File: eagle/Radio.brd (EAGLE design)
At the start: 100 x 80 mm, 105 parts, among them J500 2060-402, J501 2060-402, J920 2060-402, J921 2060-402, Q210 32.768kHz, Q610 32.768kHz, Q900 BSS123, U100 LP38693, U200 MSP430G2553, U300 IRF7103, U500 TPA2016D2, U900 EA_DOGMXXX-A, U910 PCA8574, U920 PCA9632TK, U930 IRF7309, U940 OPT3001, X100 2510-5, X110 2510-5

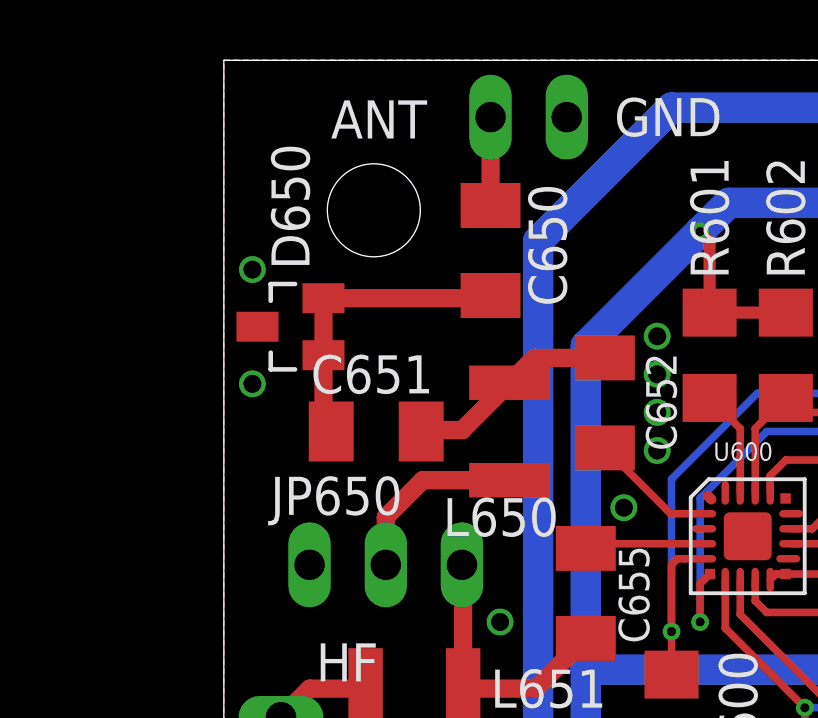
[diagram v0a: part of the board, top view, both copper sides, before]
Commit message: CHG: eagle schemetics and layout to solve issue with diode on antenna
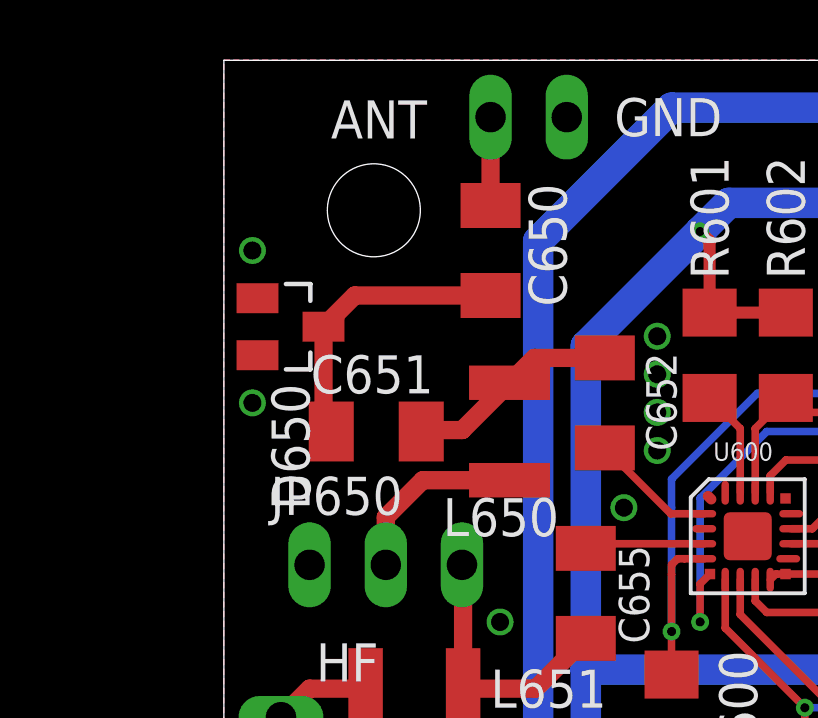
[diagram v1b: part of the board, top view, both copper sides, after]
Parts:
- turned D650 to 270 degrees
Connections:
- net GND: now also D650.1, D650.2; no longer D650.3
- net N$2: now also D650.3; no longer D650.1, D650.2
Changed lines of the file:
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@@
 <attribute name="VALUE" x="43.4975" y="35.8775" size="1.27" layer="27" rot="R180"/>
 </element>
-<element name="D650" library="diode" package="SOT23" value="BAT54S" x="2.2225" y="71.12" smashed="yes" rot="R90">
-<attribute name="NAME" x="2.8575" y="73.025" size="1.27" layer="25" rot="R90"/>
-<attribute name="VALUE" x="5.3975" y="69.215" size="1.27" layer="27" rot="R90"/>
+<element name="D650" library="diode" package="SOT23" value="BAT54S" x="2.2225" y="71.12" smashed="yes" rot="R270">
+<attribute name="NAME" x="1.5875" y="69.215" size="1.27" layer="25" rot="R270"/>
+<attribute name="VALUE" x="-0.9525" y="73.025" size="1.27" layer="27" rot="R270"/>
 </element>
 <element name="R901" library="rcl" package="R1206" value="1k" x="86.36" y="48.26" smashed="yes" rot="R270">
@@
 <via x="4.7625" y="50.4825" extent="1-16" drill="0.6" diameter="0.9"/>
 <via x="4.1275" y="51.435" extent="1-16" drill="0.6" diameter="0.9"/>
-<via x="0.9525" y="69.215" extent="1-16" drill="0.6" diameter="0.9"/>
+<via x="0.9525" y="68.58" extent="1-16" drill="0.6" diameter="0.9"/>
 <via x="80.3275" y="55.88" extent="1-16" drill="0.6" diameter="0.9"/>
 <via x="81.5975" y="55.245" extent="1-16" drill="0.6" diameter="0.9"/>
@@
 <contactref element="C654" pad="2"/>
 <contactref element="C653" pad="2"/>
-<contactref element="D650" pad="3"/>
 <contactref element="ANT" pad="1"/>
 <via x="4.1275" y="53.975" extent="1-16" drill="0.6" diameter="0.9"/>
@@
 <via x="14.44625" y="69.5325" extent="1-16" drill="0.6" diameter="0.9"/>
 <via x="10.795" y="39.37" extent="1-16" drill="0.6" diameter="0.9"/>
-<via x="0.9525" y="73.025" extent="1-16" drill="0.6" diameter="0.9"/>
+<via x="0.9525" y="73.66" extent="1-16" drill="0.6" diameter="0.9"/>
 <via x="7.3025" y="38.4175" extent="1-16" drill="0.6" diameter="0.9"/>
 <via x="8.5725" y="38.4175" extent="1-16" drill="0.6" diameter="0.9"/>
@@
 <contactref element="U940" pad="7"/>
 <wire x1="50" y1="23" x2="49.005" y2="23" width="0.254" layer="16"/>
+<contactref element="D650" pad="2"/>
+<contactref element="D650" pad="1"/>
 </signal>
 <signal name="+5V">
@@
 </signal>
 <signal name="N$2">
+<contactref element="C651" pad="2"/>
+<wire x1="3.58" y1="67.6275" x2="3.3225" y2="67.6275" width="0.6096" layer="1"/>
 <contactref element="C650" pad="2"/>
-<contactref element="D650" pad="2"/>
-<wire x1="3.3225" y1="72.07" x2="8.8" y2="72.07" width="0.6096" layer="1"/>
-<wire x1="8.8" y1="72.07" x2="8.89" y2="72.16" width="0.6096" layer="1"/>
-<contactref element="C651" pad="2"/>
-<contactref element="D650" pad="1"/>
+<contactref element="D650" pad="3"/>
 <wire x1="3.58" y1="67.6275" x2="3.3225" y2="67.6275" width="0.6096" layer="1"/>
-<wire x1="3.3225" y1="67.6275" x2="3.3225" y2="70.17" width="0.6096" layer="1"/>
-<wire x1="3.3225" y1="70.17" x2="3.3225" y2="72.07" width="0.6096" layer="1"/>
+<wire x1="3.3225" y1="67.6275" x2="3.3225" y2="71.12" width="0.6096" layer="1"/>
+<wire x1="3.3225" y1="71.12" x2="4.3625" y2="72.16" width="0.6096" layer="1"/>
+<wire x1="4.3625" y1="72.16" x2="8.89" y2="72.16" width="0.6096" layer="1"/>
 </signal>
 <signal name="N$32">

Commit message: CHG: Finishing Layout and Schemetics
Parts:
- added R921, R922, R923: 1k, rcl:R1206
- moved C920 10.4 mm to (92.4, 53.0), turned to 0 degrees
- moved U920 3.82 mm to (90.2, 48.3), turned to 0 degrees
- moved J920 0.32 mm to (91.1, 36.8)
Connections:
- new net N$25: R921.1, U920.2
- new net N$45: J920.B-2, R922.2
- new net N$46: J921.B-2, R923.2
- net +5V: no longer R901.1
- net GND: now also R901.1
- net N$3: now also R923.1, U920.4; no longer J920.B-1, U920.2
- net N$44: now also J920.B-1, R921.2; no longer J921.B-2, U920.4
- net N$5: now also R922.1; no longer J920.B-2
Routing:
- net N$25: track 0.00 -> 15.7 mm
- net N$46: track 0.00 -> 15.3 mm
- net N$3: track 15.6 -> 3.72 mm
- net N$44: track 15.5 -> 4.01 mm
- net +5V: track 386.2 -> 375.0 mm
- net SCL_5V: track 165.9 -> 177.0 mm
- net +5_PCA: track 71.3 -> 61.2 mm
- net SDA_5V: track 173.7 -> 183.7 mm
- net N$45: track 0.00 -> 4.95 mm
- net EN1_TAST: track 63.6 -> 62.9 mm
- net N$5: track 7.26 -> 6.60 mm
- net LCD_BACKLIGHT: track 5.46 -> 6.00 mm

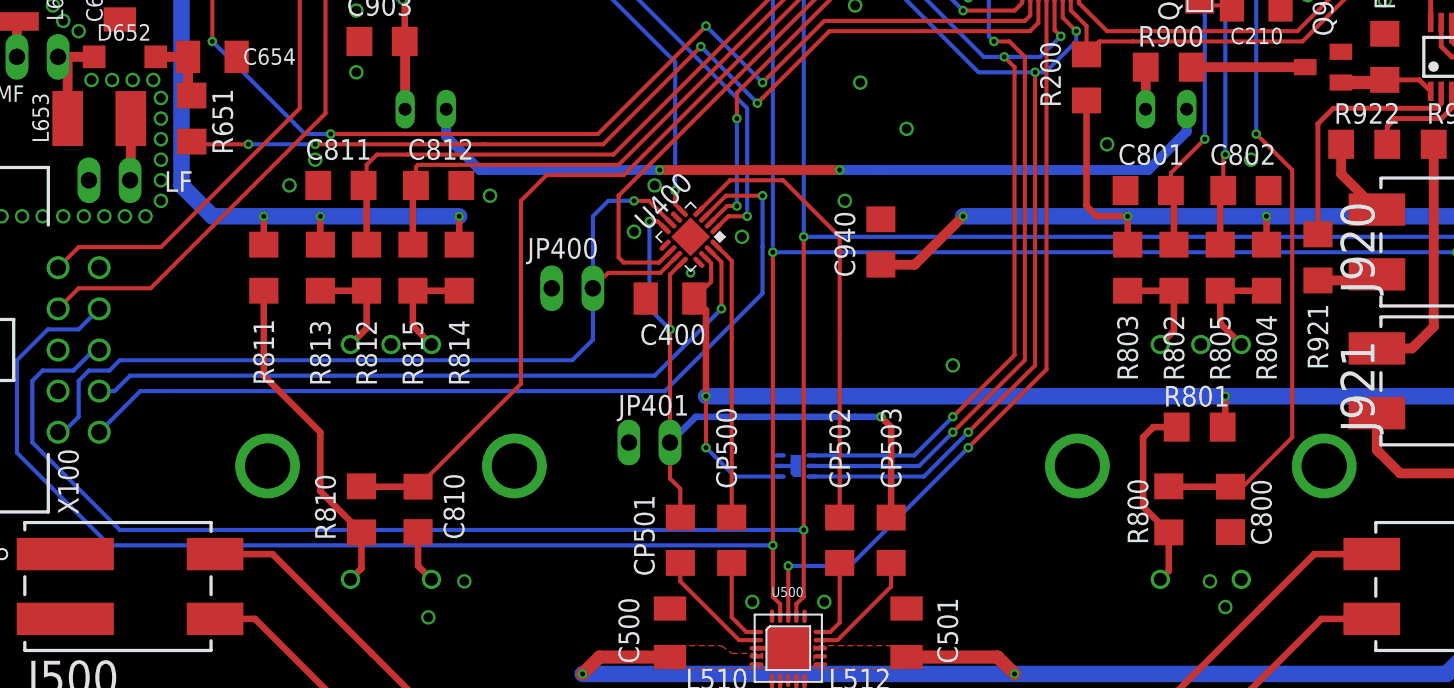
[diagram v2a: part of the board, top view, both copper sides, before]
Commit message: CHG: solved some problems on pcb updated encoder footprint, further updated schemetics and changed pull up resitor to an pull down for lcd backlight controll
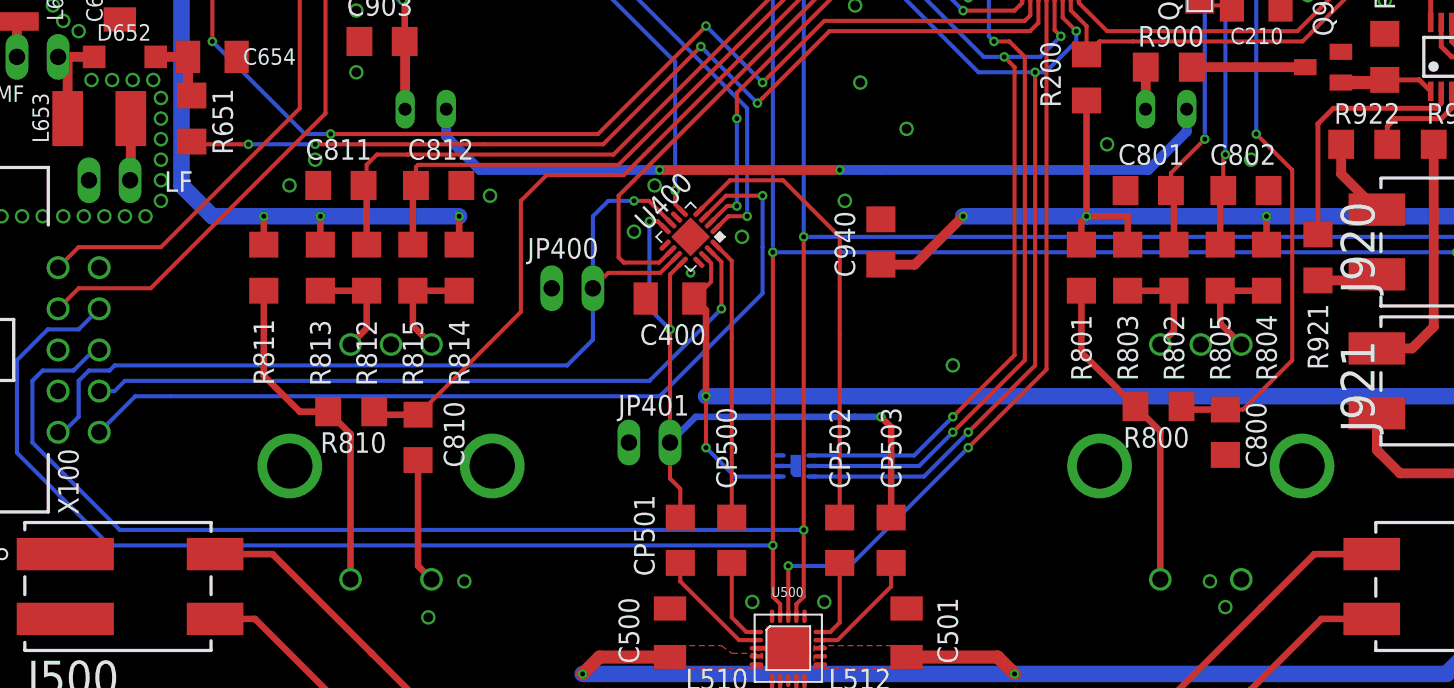
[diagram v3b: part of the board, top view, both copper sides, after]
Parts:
- U910: device Radio Projekt:TSSOP16 -> Radio Projekt:PCA8574_TSSOP16
- moved R801 12.3 mm to (67.6, 35.2), turned to 90 degrees
- moved R800 6.38 mm to (72.4, 26.7), turned to 180 degrees
- moved R810 6.07 mm to (22.5, 26.4), turned to 0 degrees
- moved C800 4.77 mm to (76.5, 25.1)
- moved C810 4.45 mm to (26.7, 24.8)
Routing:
- net N$36: track 12.0 -> 19.8 mm
- net EN1_TAST: track 62.9 -> 57.4 mm
- net EN2_TAST: track 60.6 -> 55.5 mm
- net GND: track 7.06 -> 11.5 mm
- net AUX_LIN: track 45.0 -> 44.4 mm
- net +3V3: track 396.9 -> 397.2 mm, vias 15 -> 14

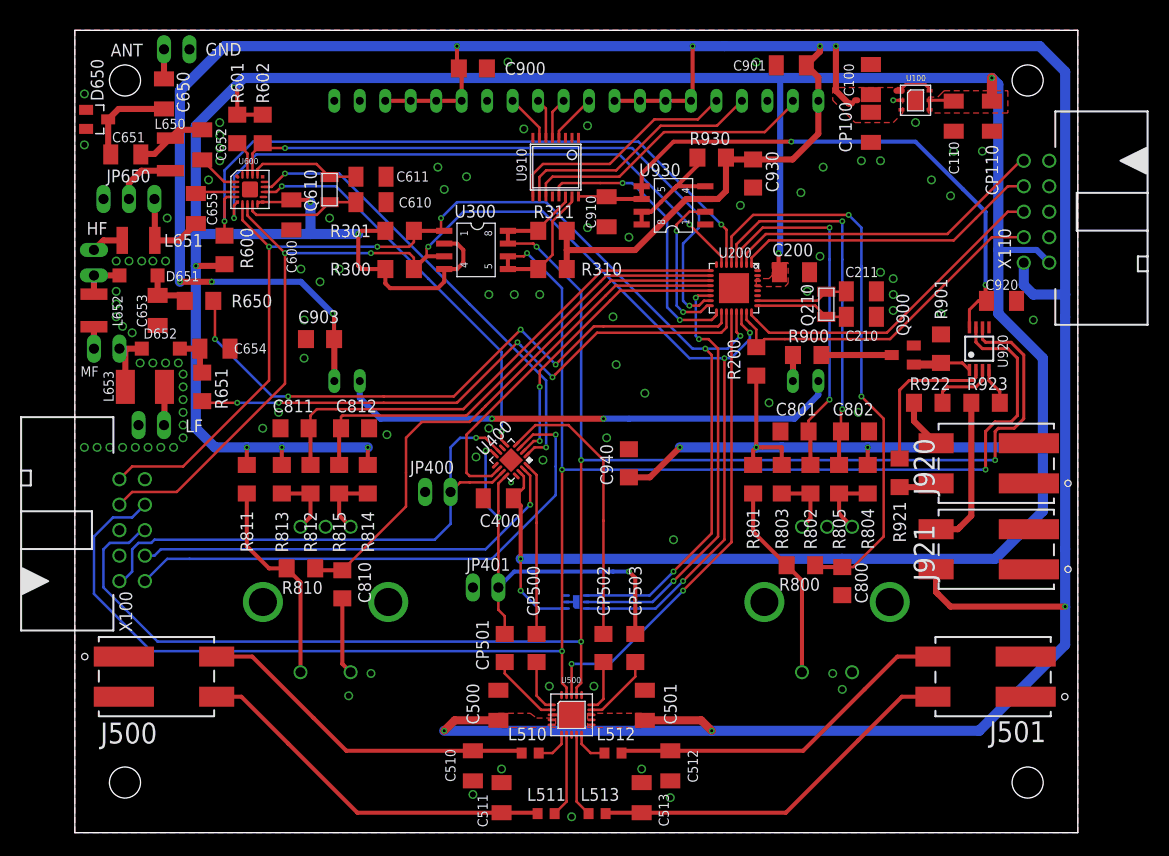
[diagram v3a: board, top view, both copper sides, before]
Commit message: CHG: updated radio schematics and pcb with test pads
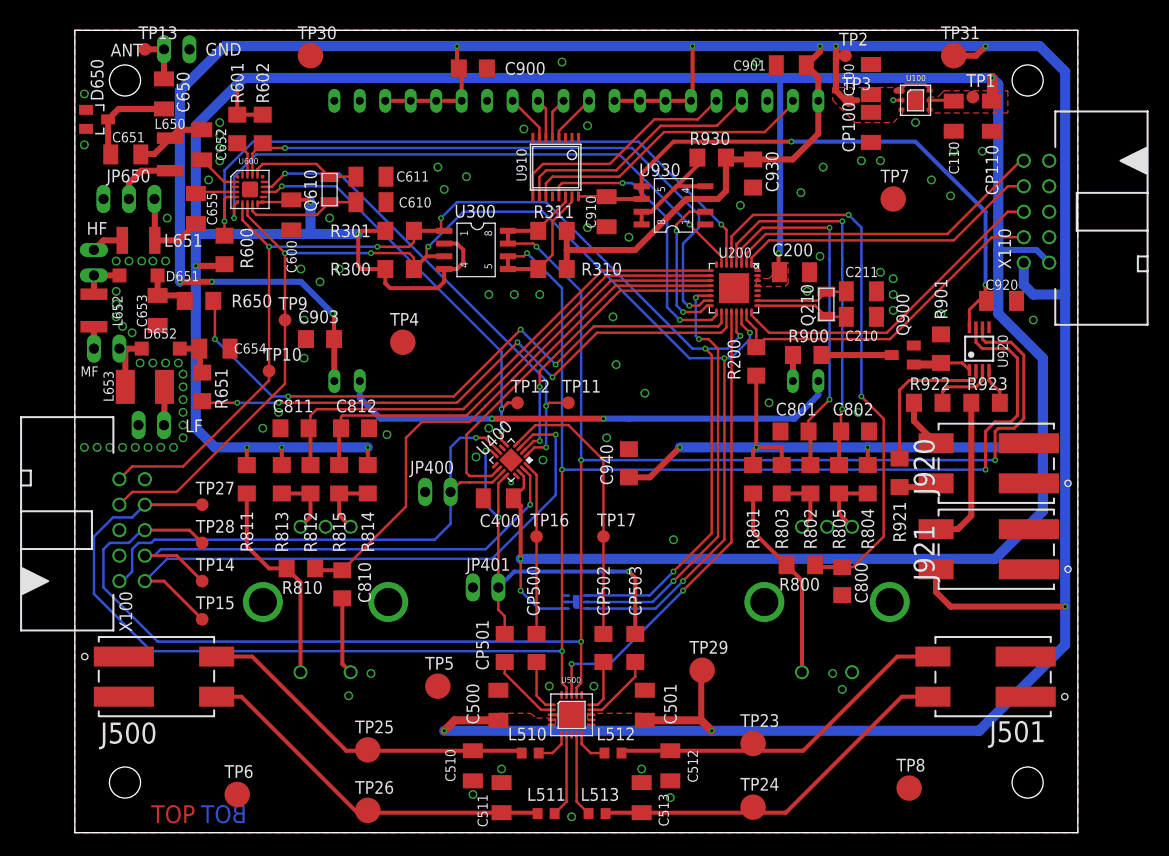
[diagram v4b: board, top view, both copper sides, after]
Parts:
- added TP1, TP10, TP11, TP12, TP13, TP14, TP15, TP16, TP17, TP2, TP27, TP28, TP3, TP9: PTR1B1,27, testpad:B1,27
- added TP23, TP24, TP25, TP26, TP29, TP30, TP31, TP4, TP5, TP6, TP7, TP8: PTR1B2,54, testpad:B2,54
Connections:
- removed net N$13: C510.2, J500.B-1, L510.1
- removed net N$14: C511.2, J500.B-2, L511.1
- removed net N$15: C512.1, J501.B-2, L512.1
- removed net N$16: C513.1, J501.B-1, L513.1
- removed net N$41: ANT.2, C650.1
- new net AMP_OUTL+: C510.2, J500.B-1, L510.1, TP25.TP
- new net AMP_OUTL-: C511.2, J500.B-2, L511.1, TP26.TP
- new net AMP_OUTR+: C512.1, J501.B-2, L512.1, TP23.TP
- new net AMP_OUTR-: C513.1, J501.B-1, L513.1, TP24.TP
- new net ANT_FM: ANT.2, C650.1, TP13.TP
- net +3V3: now also TP1.TP
- net +5V: now also TP2.TP, TP29.TP, TP3.TP, TP31.TP
- net AMP_LIN: now also TP16.TP
- net AMP_RIN: now also TP17.TP
- net AUX_LIN: now also TP14.TP
- net AUX_RIN: now also TP15.TP
- net GND: now also TP30.TP, TP4.TP, TP5.TP, TP6.TP, TP7.TP, TP8.TP
- net SCL_3.3V: now also TP10.TP
- net SCL_5V: now also TP28.TP
- net SDA_3.3V: now also TP9.TP
- net SDA_5V: now also TP27.TP
- net SI_LOUT: now also TP11.TP
- net SI_ROUT: now also TP12.TP
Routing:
- net AMP_OUTR-: track 0.00 -> 38.0 mm
- net N$16: track 37.2 -> 0.00 mm
- net AMP_OUTL-: track 0.00 -> 37.1 mm
- net N$14: track 36.8 -> 0.00 mm
- net AMP_OUTR+: track 0.00 -> 35.8 mm
- net N$15: track 35.0 -> 0.00 mm
- net AMP_OUTL+: track 0.00 -> 34.8 mm
- net N$13: track 34.4 -> 0.00 mm
- net +5V: track 375.0 -> 389.8 mm, vias 10 -> 11
- net AUX_RIN: track 54.7 -> 62.0 mm
- net AUX_LIN: track 44.4 -> 51.2 mm
- net SCL_5V: track 177.0 -> 183.2 mm
- net SDA_5V: track 183.7 -> 189.4 mm
- net ANT_FM: track 0.00 -> 4.85 mm
- net N$41: track 2.95 -> 0.00 mm
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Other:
- board text added: "BOT"
- board text added: "TOP"

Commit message: CHG: improved layout for final releas
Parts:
- moved TP11 12.3 mm to (37.8, 47.3)
- moved TP12 10.4 mm to (34.3, 46.4)
- moved TP17 5.84 mm to (47.3, 27.3)
- moved TP4 4.69 mm to (36.8, 51.1)
- moved TP16 0.32 mm to (46.0, 29.8)
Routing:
- net +5V: track 389.8 -> 336.9 mm, vias 11 -> 8
- net +3V3: track 397.2 -> 377.5 mm, vias 14 -> 15
- net SI_INT: track 62.4 -> 55.8 mm
- net PCA_INT: track 28.3 -> 21.8 mm
- net N$26: track 50.6 -> 55.3 mm, vias 2 -> 1
- net !SI_RST: track 68.3 -> 64.1 mm
- net AUX_RIN: track 62.0 -> 58.3 mm
- net !OPT_INT: track 42.7 -> 46.0 mm
- net SCL_3.3V: track 131.5 -> 128.7 mm
- net AMP_RIN: track 28.3 -> 30.9 mm, vias 0 -> 2
- net EN1_A: track 35.8 -> 38.3 mm
- net !SI_EN: track 60.4 -> 57.9 mm
- net EN1_B: track 37.9 -> 40.0 mm
- net SDA_3.3V: track 137.9 -> 135.9 mm, vias 6 -> 4
- net AUX_LIN: track 51.2 -> 49.7 mm
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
